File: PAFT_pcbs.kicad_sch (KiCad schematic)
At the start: 5 parts, among them J1 Conn_01x03, J2 Conn_01x03, U2 DRV8848

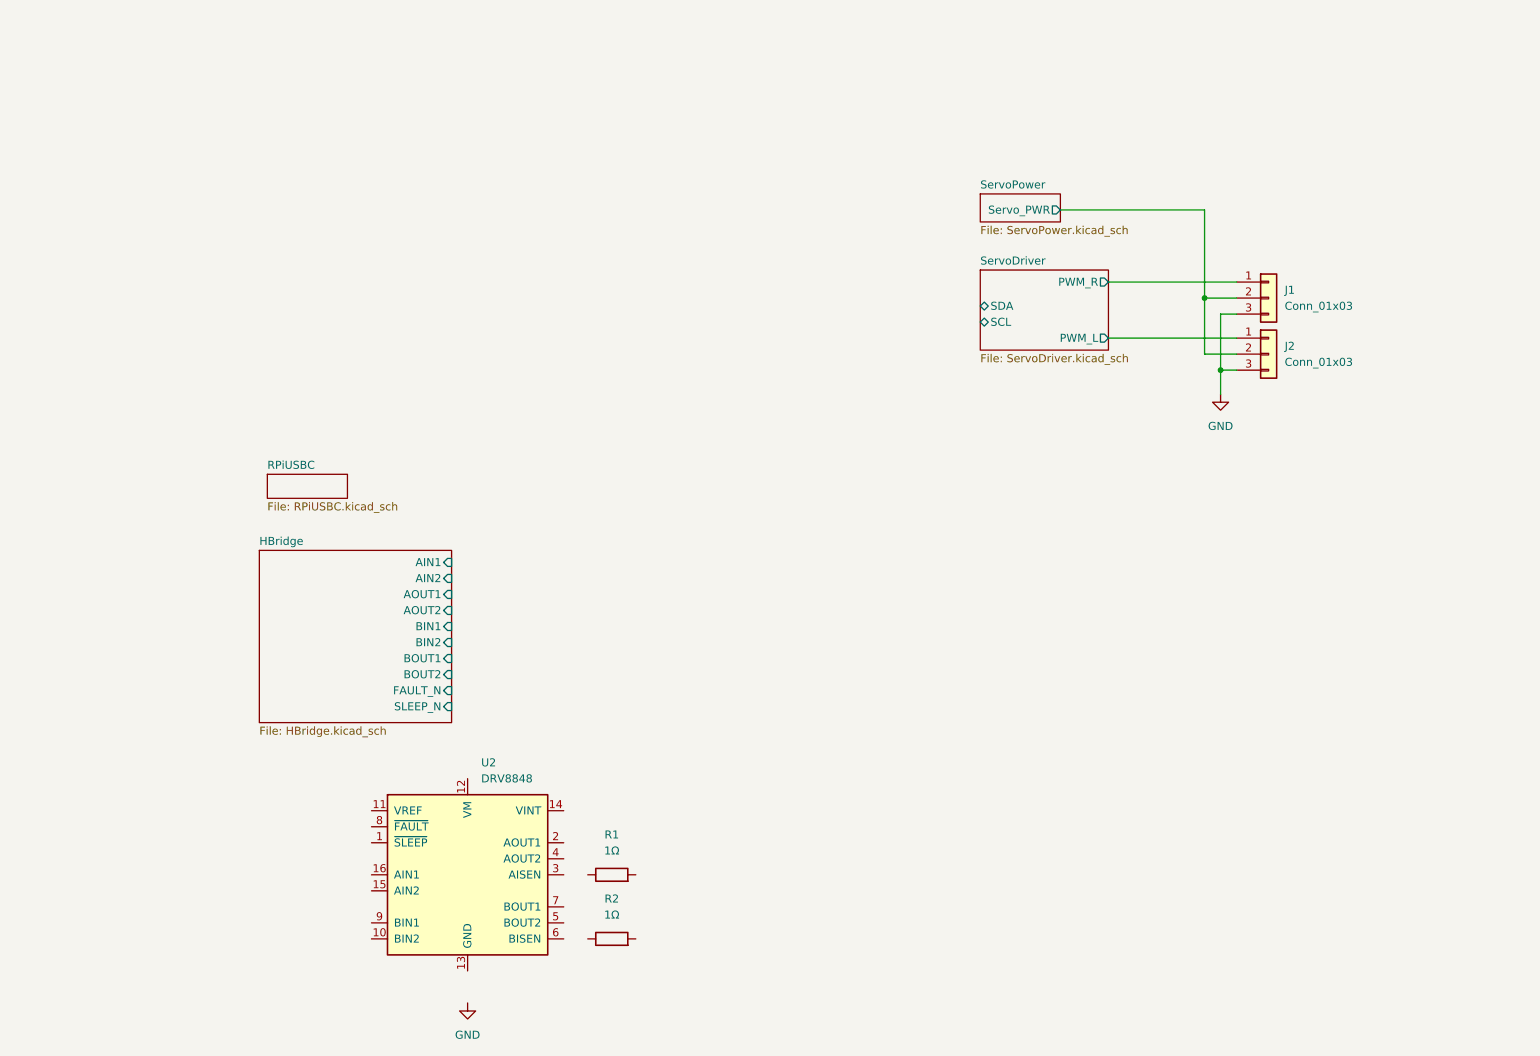
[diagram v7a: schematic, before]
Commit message: Added voltage/signal test points
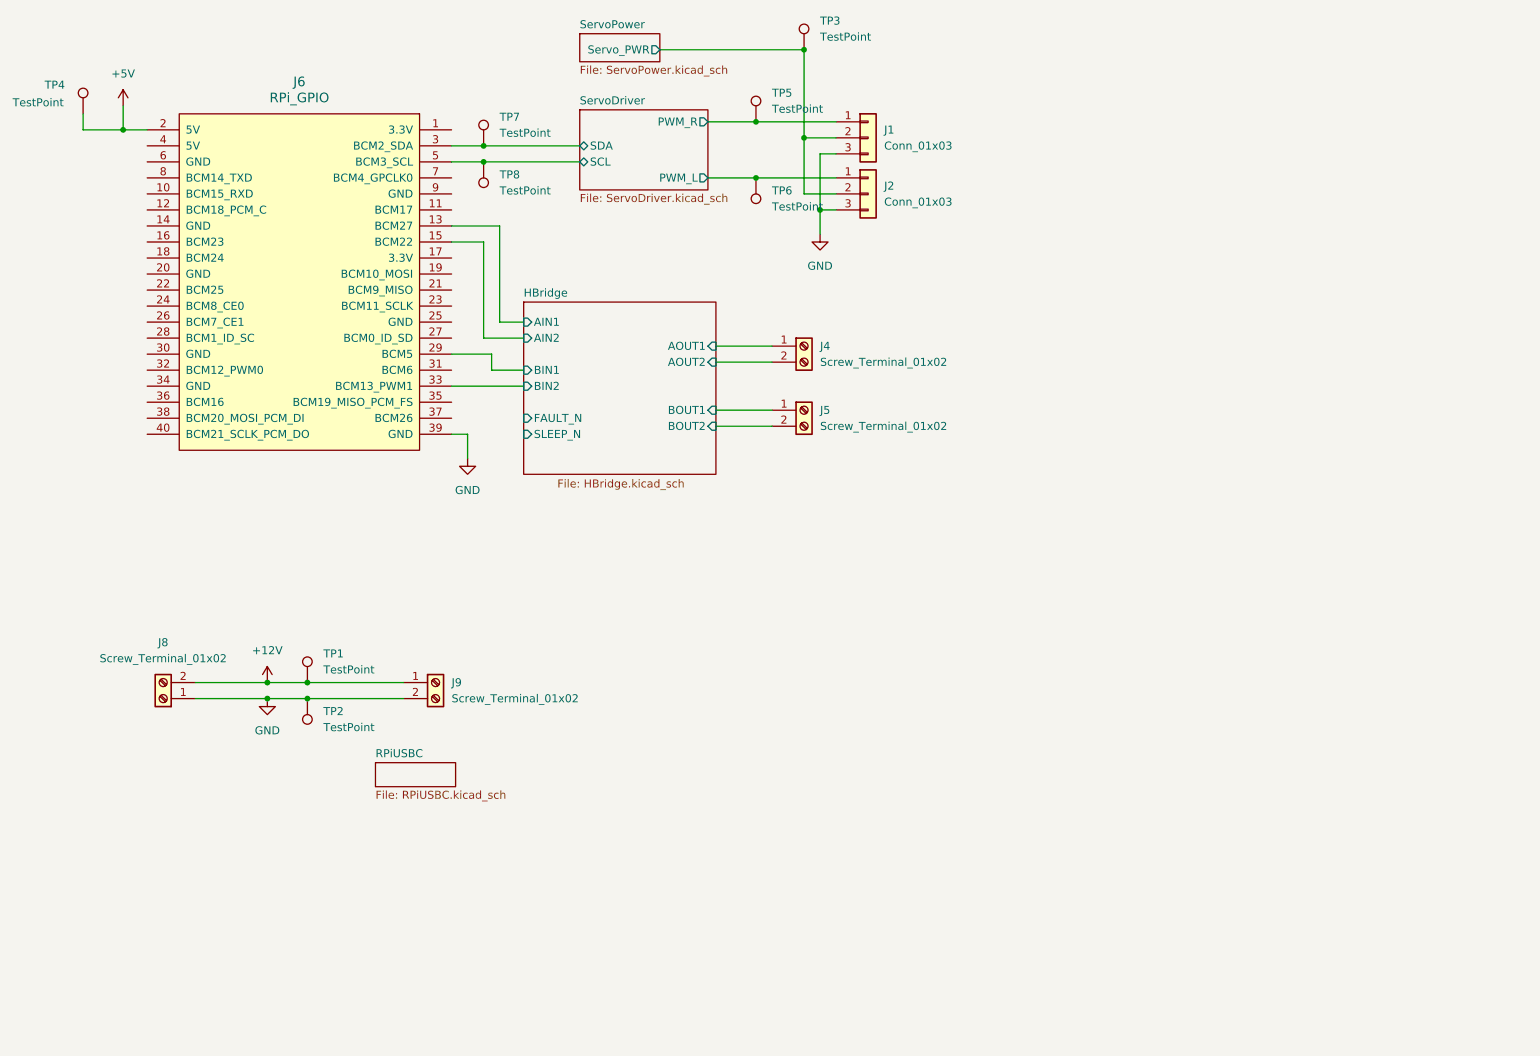
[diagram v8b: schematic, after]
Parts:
- removed R1, R2: 1Ω, symbol Device:R
- removed U2: DRV8848, Package_SO:TSSOP-16-1EP_4.4x5mm_P0.65mm, symbol Driver_Motor:DRV8848
- added J4, J5, J8, J9: Screw_Terminal_01x02, TerminalBlock:TerminalBlock_MaiXu_MX126-5.0-02P_1x02_P5.00mm, symbol Connector:Screw_Terminal_01x02
- added J6: RPi_GPIO, symbol RPi_Hat:RPi_GPIO
- added TP1, TP2, TP3, TP4, TP5, TP6, TP7, TP8: TestPoint, symbol Connector:TestPoint
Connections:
- net GND: now also J6.39 (GND), J8.1 (Pin_1), J9.2 (Pin_2), TP2.1
- net HBridge/AIN1: now also J6.13 (BCM27)
- net HBridge/AIN2: now also J6.15 (BCM22)
- net HBridge/AOUT1: now also J4.1 (Pin_1)
- net HBridge/AOUT2: now also J4.2 (Pin_2)
- net HBridge/BIN1: now also J6.29 (BCM5)
- net HBridge/BIN2: now also J6.33 (BCM13_PWM1)
- net HBridge/BOUT1: now also J5.1 (Pin_1)
- net HBridge/BOUT2: now also J5.2 (Pin_2)
- net ServoDriver/PWM_L: now also TP6.1
- net ServoDriver/PWM_R: now also TP5.1
- net ServoDriver/SCL: now also J6.5 (BCM3_SCL), TP8.1
- net ServoDriver/SDA: now also J6.3 (BCM2_SDA), TP7.1
- net ServoPower/Servo_PWR: now also TP3.1
- new net +12V: J8.2 (Pin_2), J9.1 (Pin_1), TP1.1
- new net +5V: J6.2 (5V), TP4.1
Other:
- moved on the sheet: J1, J2
